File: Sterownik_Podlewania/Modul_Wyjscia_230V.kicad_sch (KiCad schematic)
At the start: 10 parts, among them J2 Screw_Terminal_01x02, K2 SANYOU_SRD_Form_C, Q2 BC547, SW8 SW_Nidec_CAS-120A1

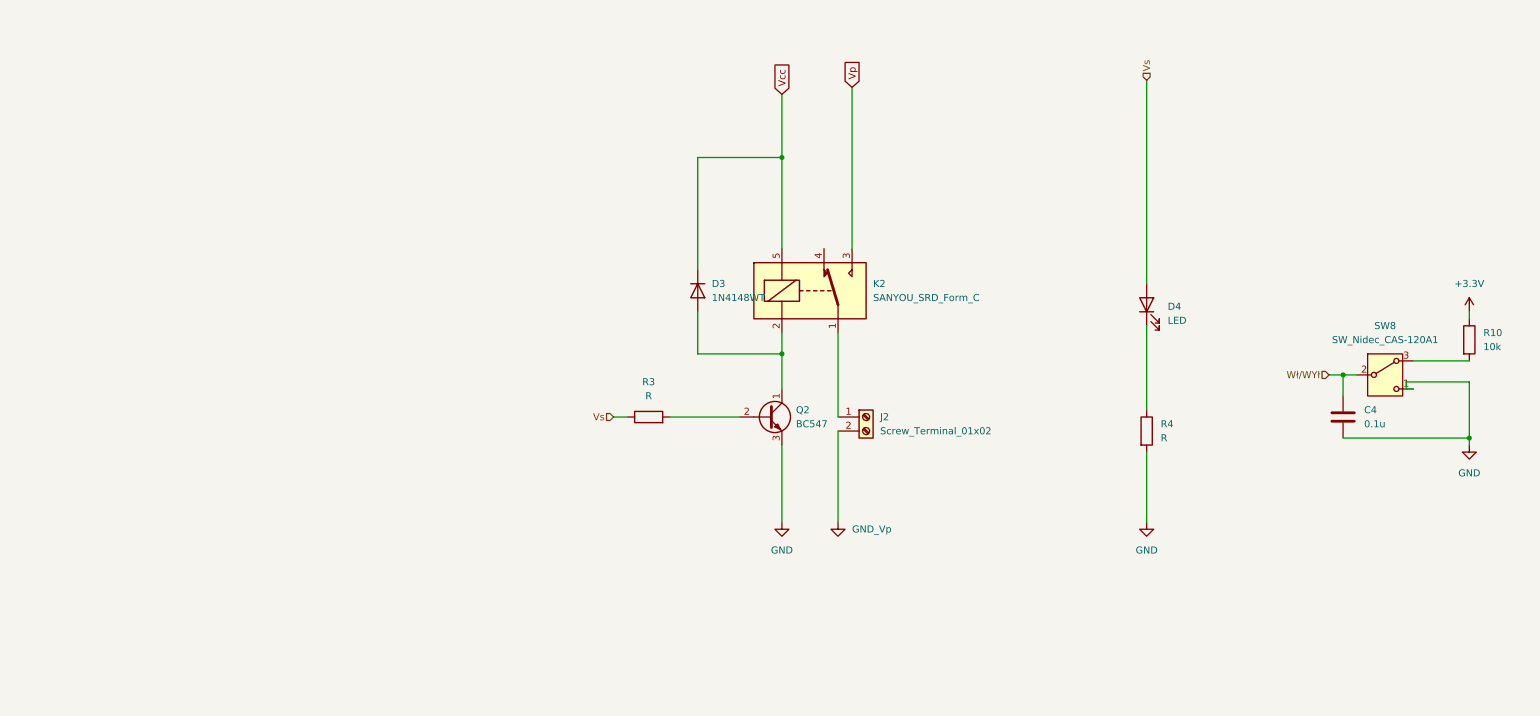
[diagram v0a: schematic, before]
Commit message: Dodanie większośi footprinów, dodanie osobno sekcji na 230V, dodanie jacka DC
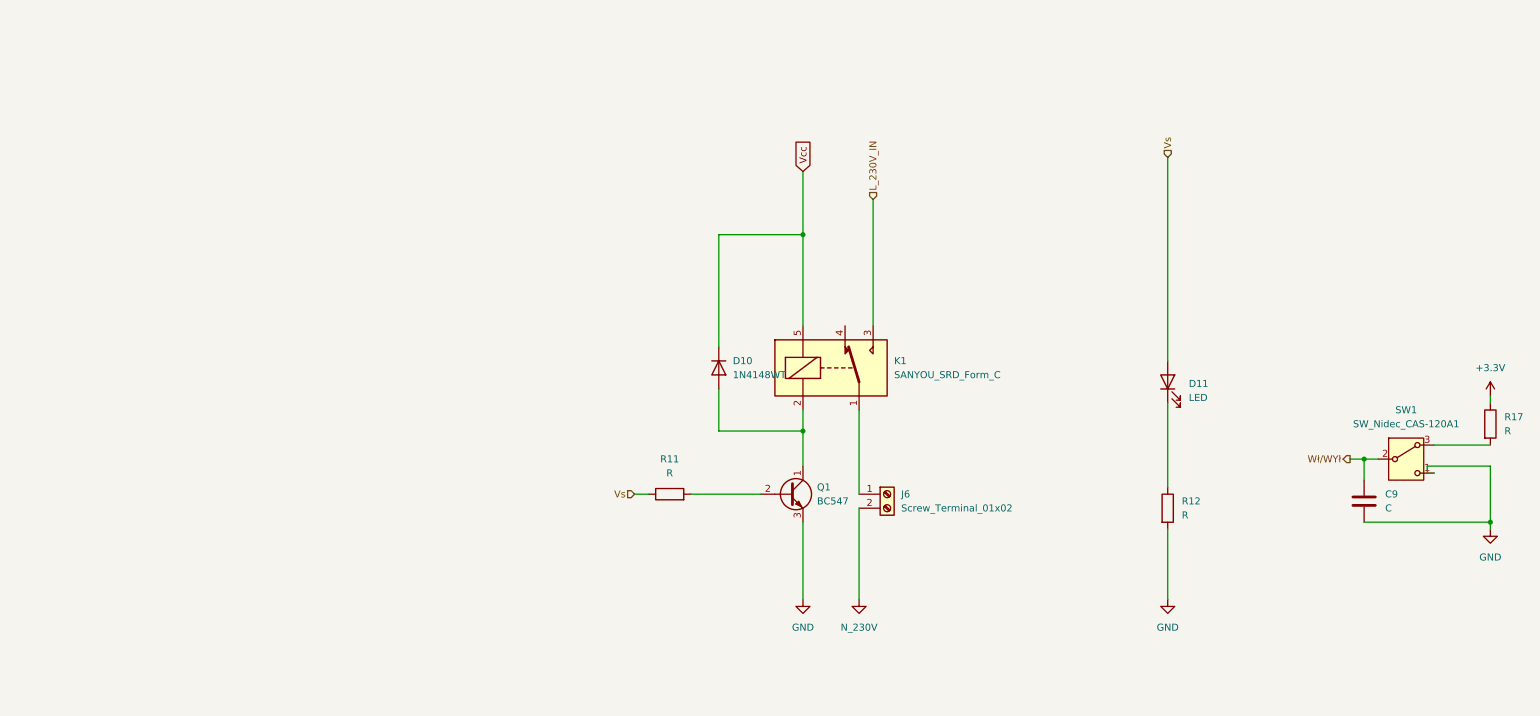
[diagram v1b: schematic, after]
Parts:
- removed C4: 0.1u, Capacitor_SMD:C_1206_3216Metric, symbol Device:C
- removed D3: 1N4148WT, Diode_SMD:D_SOD-523, symbol Diode:1N4148WT
- removed D4: LED, LED_SMD:LED_1206_3216Metric, symbol Device:LED
- removed J2: Screw_Terminal_01x02, TerminalBlock:TerminalBlock_MaiXu_MX126-5.0-02P_1x02_P5.00mm, symbol Connector:Screw_Terminal_01x02
- removed K2: SANYOU_SRD_Form_C, Relay_THT:Relay_SPDT_SANYOU_SRD_Series_Form_C, symbol Relay:SANYOU_SRD_Form_C
- removed Q2: BC547, Package_TO_SOT_THT:TO-92_Inline, symbol Transistor_BJT:BC547
- removed R10: 10k, Resistor_SMD:R_1206_3216Metric, symbol Device:R
- removed R3, R4: R, Resistor_SMD:R_1206_3216Metric, symbol Device:R
- removed SW8: SW_Nidec_CAS-120A1, Button_Switch_SMD:Nidec_Copal_CAS-120A, symbol Switch:SW_Nidec_CAS-120A1
- added C9: C, symbol Device:C
- added D10: 1N4148WT, Diode_SMD:D_SOD-523, symbol Diode:1N4148WT
- added D11: LED, LED_SMD:LED_1206_3216Metric, symbol Device:LED
- added J6: Screw_Terminal_01x02, TerminalBlock:TerminalBlock_Wuerth_691311400102_P7.62mm, symbol Connector:Screw_Terminal_01x02
- added K1: SANYOU_SRD_Form_C, Relay_THT:Relay_SPDT_SANYOU_SRD_Series_Form_C, symbol Relay:SANYOU_SRD_Form_C
- added Q1: BC547, Package_TO_SOT_THT:TO-92_Inline, symbol Transistor_BJT:BC547
- added R11, R12, R17: R, Resistor_SMD:R_1206_3216Metric, symbol Device:R
- added SW1: SW_Nidec_CAS-120A1, Button_Switch_SMD:Nidec_Copal_CAS-120A, symbol Switch:SW_Nidec_CAS-120A1
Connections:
- net +3.3V: now also R17.1
- net GND: now also C9.2, Q1.3 (E), R12.2, SW1.1 (C)
- net Vcc: now also D10.1 (K), K1.5
- net Vs: now also D11.2 (A), R11.1
- net Wł/WYł: now also C9.1, SW1.2 (B)
- new net: D10.2 (A), K1.2, Q1.1 (C)
- new net: J6.1 (Pin_1), K1.1
- new net: R17.2, SW1.3 (A)
- new net: Q1.2 (B), R11.2
- new net: D11.1 (K), R12.1
- new net L_230V_IN: K1.3
- new net N_230V: J6.2 (Pin_2)

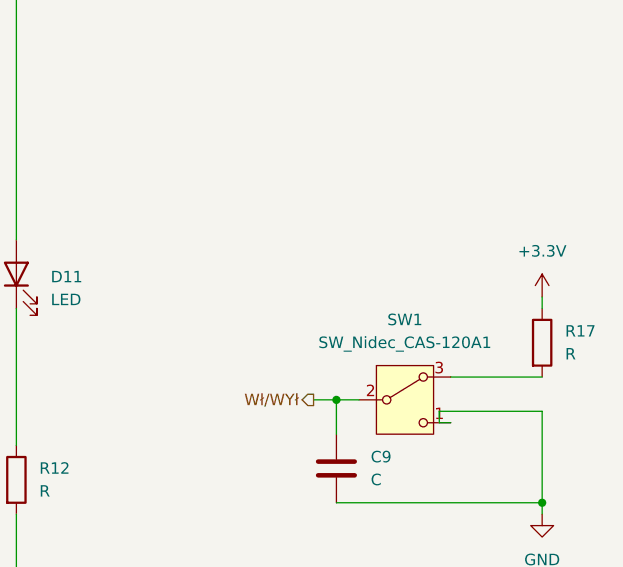
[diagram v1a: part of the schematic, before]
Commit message: Dodanie dokumentacji przełączników, sprawdzenie konwertera I2C, dodanie sekcji przełącznika, dodanie DIP swticha do przełączania zasialania zew, wydzielenie sekcji zasilania
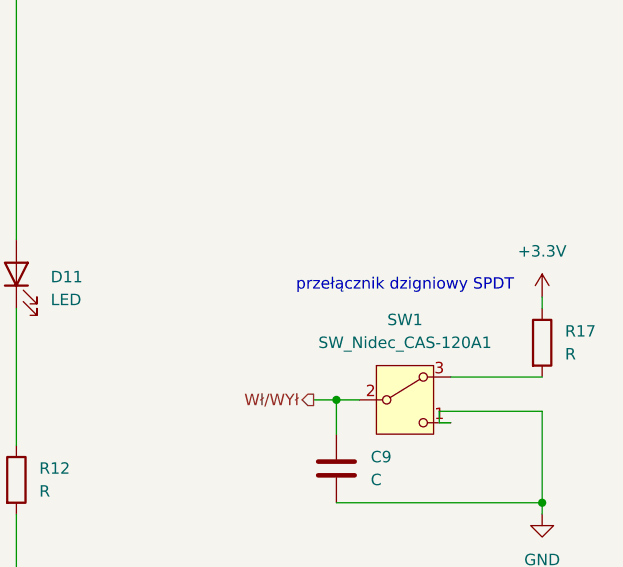
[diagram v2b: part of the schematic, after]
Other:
- note added: "przełącznik dzigniowy SPDT"
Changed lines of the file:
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@@
 	(generator_version "9.0")
 	(paper "A4")
+	(text "przełącznik dzigniowy SPDT "
+		(exclude_from_sim no)
+		(at 250.19 91.44 0)
+		(effects
+			(font
+				(size 1.27 1.27)
+			)
+			(href "https://botland.com.pl/przelaczniki-dzwigienkowe/2478-przelacznik-dzwigniowy-on-on-250v-3a-5szt-5904422356361.html")
+		)
+	)
 	(junction
 		(at 265.43 115.57)

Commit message: Poprawki estetyczne schematu
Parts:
- removed C9: C, symbol Device:C
- removed D10: 1N4148WT, Diode_SMD:D_SOD-523, symbol Diode:1N4148WT
- removed D11: LED, LED_SMD:LED_1206_3216Metric, symbol Device:LED
- removed J6: Screw_Terminal_01x02, TerminalBlock:TerminalBlock_Wuerth_691311400102_P7.62mm, symbol Connector:Screw_Terminal_01x02
- removed K1: SANYOU_SRD_Form_C, Relay_THT:Relay_SPDT_SANYOU_SRD_Series_Form_C, symbol Relay:SANYOU_SRD_Form_C
- removed Q1: BC547, Package_TO_SOT_THT:TO-92_Inline, symbol Transistor_BJT:BC547
- removed R11, R12, R17: R, Resistor_SMD:R_1206_3216Metric, symbol Device:R
- removed SW1: SW_Nidec_CAS-120A1, Button_Switch_SMD:Nidec_Copal_CAS-120A, symbol Switch:SW_Nidec_CAS-120A1
- added D15: LED, LED_SMD:LED_1206_3216Metric, symbol Device:LED
- added D9: 1N4148WT, Diode_SMD:D_SOD-523, symbol Diode:1N4148WT
- added J1: Screw_Terminal_01x02, TerminalBlock:TerminalBlock_MaiXu_MX126-5.0-02P_1x02_P5.00mm, symbol Connector:Screw_Terminal_01x02
- added K3: SANYOU_SRD_Form_C, Relay_THT:Relay_SPDT_SANYOU_SRD_Series_Form_C, symbol Relay:SANYOU_SRD_Form_C
- added Q3: BC547, Package_TO_SOT_THT:TO-92_Inline, symbol Transistor_BJT:BC547
- added R10: 680, Resistor_SMD:R_1206_3216Metric, symbol Device:R
- added R13: R, Resistor_SMD:R_1206_3216Metric, symbol Device:R
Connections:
- net GND: now also Q3.3 (E), R13.2
- net L_230V_IN: now also K3.3
- net N_230V: now also J1.2 (Pin_2)
- net Vcc: now also D9.1 (K), K3.5
- net Vs: now also D15.2 (A), R10.1
- new net: D9.2 (A), K3.2, Q3.1 (C)
- new net: Q3.2 (B), R10.2
- new net: D15.1 (K), R13.1
- new net: J1.1 (Pin_1), K3.1
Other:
- added sheet Przelacznik (Przelacznik.kicad_sch)
- note removed: "przełącznik dzigniowy SPDT"

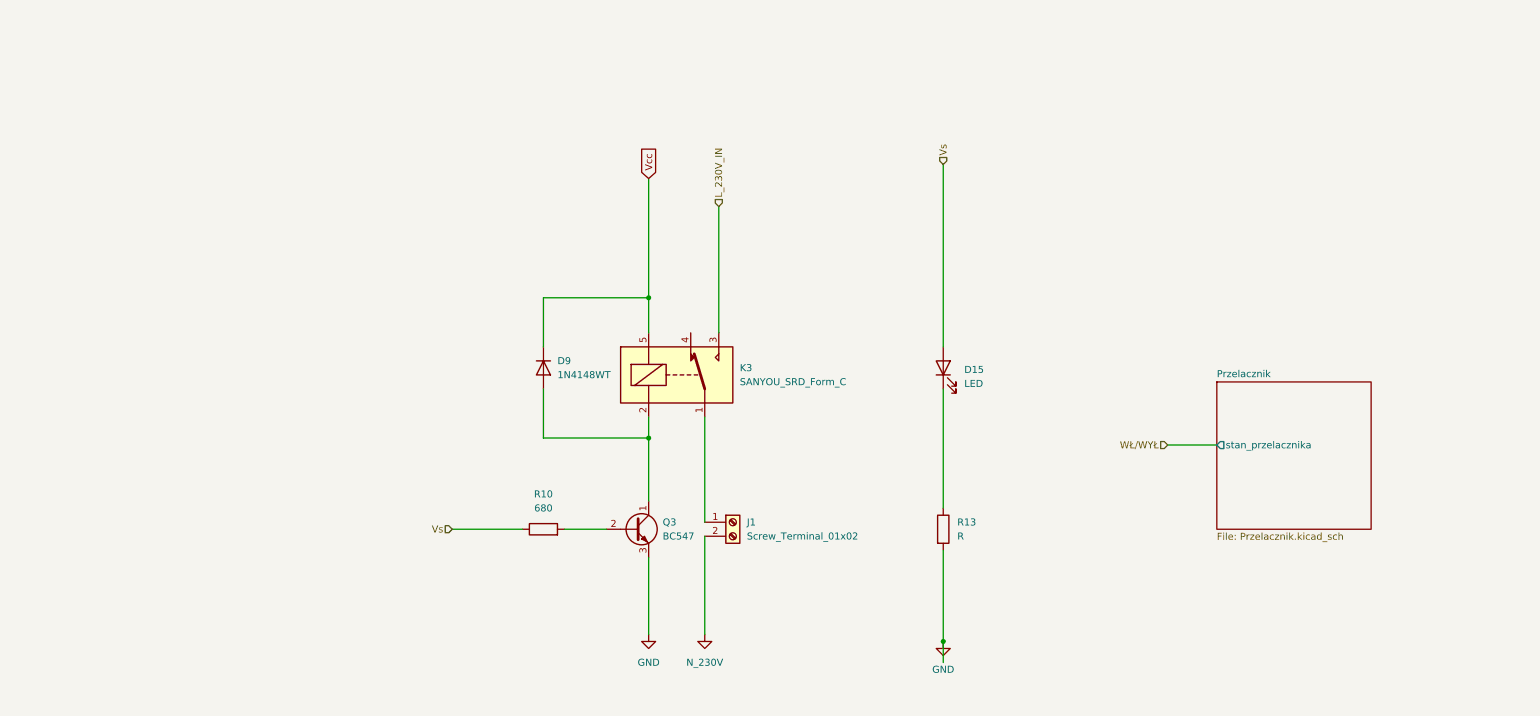
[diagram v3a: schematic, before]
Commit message: Dodanie gniazd ethernet, poprawienie większośc ERC
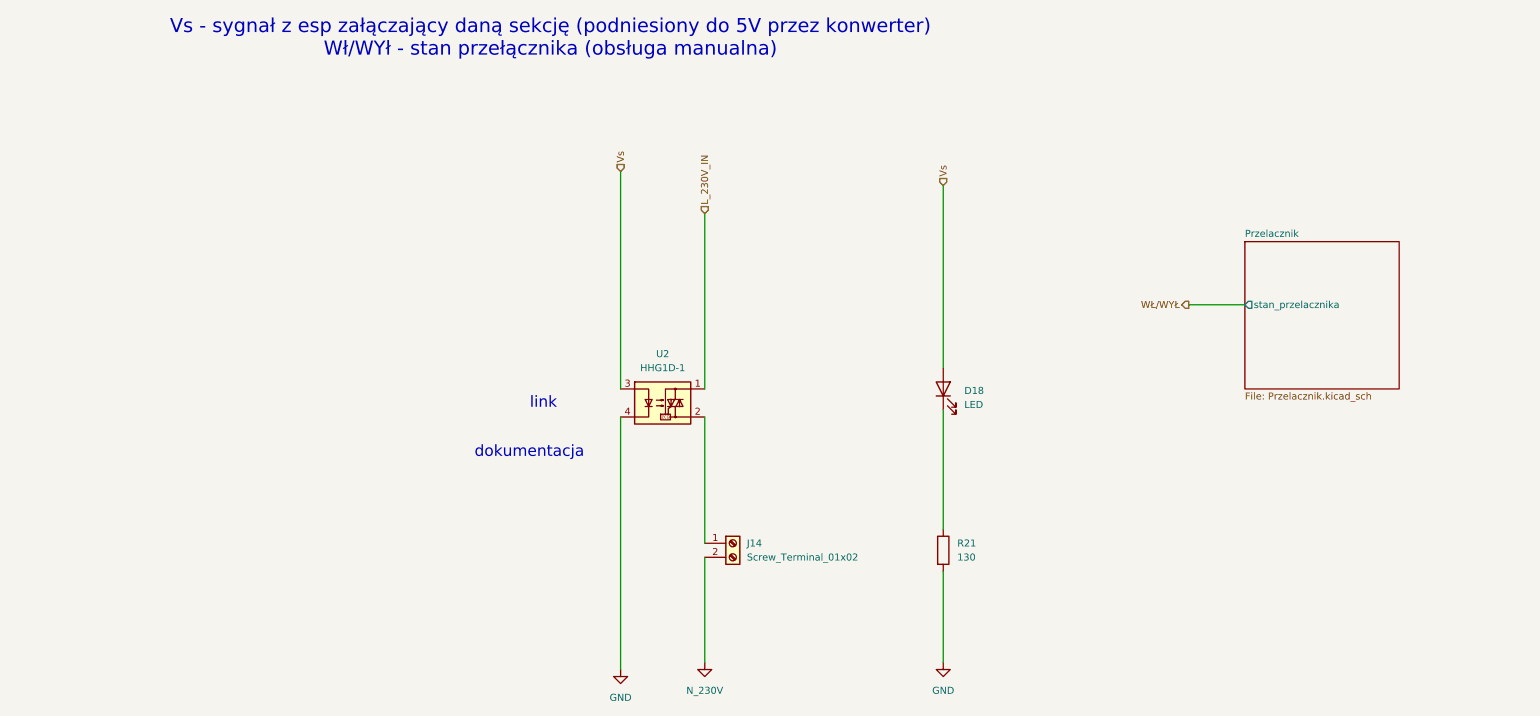
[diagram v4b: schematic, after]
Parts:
- removed D9: 1N4148WT, Diode_SMD:D_SOD-523, symbol Diode:1N4148WT
- removed K3: SANYOU_SRD_Form_C, Relay_THT:Relay_SPDT_SANYOU_SRD_Series_Form_C, symbol Relay:SANYOU_SRD_Form_C
- removed Q3: BC547, Package_TO_SOT_THT:TO-92_Inline, symbol Transistor_BJT:BC547
- removed R10: 680, Resistor_SMD:R_1206_3216Metric, symbol Device:R
- added U2: HHG1D-1, Relay_THT:Relay_NCR_HHG1D-1, symbol Relay_SolidState:HHG1D-1
- R21: renamed from R13; value R -> 130
- renumbered D15 to D18, J1 to J14
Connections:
- net GND: now also U2.4
- net L_230V_IN: now also U2.1
- net Vs: now also U2.3
- net at J14.1 (Pin_1): now also U2.2
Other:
- note added: "Vs - sygnał z esp załączający daną sekcję (podniesiony do 5V przez konwerter) Wł/WYł - stan przełącznika (obsługa manualna)"
- note added: "dokumentacja"
- note added: "link"
- title: (none) -> Sterownik podlewania V1.1
- moved on the sheet: D18, J14, R21

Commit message: Wstępny układ PCB
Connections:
- net L_230V_IN renamed 230VAC
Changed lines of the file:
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@@
-	(wire
-		(pts
-			(xy 123.19 59.69) (xy 123.19 91.44)
-		)
-		(stroke
-			(width 0)
-			(type default)
-		)
-	)
 	(wire
 		(pts
@@
 		(pts
 			(xy 166.37 124.46) (xy 166.37 140.97)
+		)
+		(stroke
+			(width 0)
+			(type default)
+		)
+	)
+	(wire
+		(pts
+			(xy 123.19 57.15) (xy 123.19 91.44)
 		)
 		(stroke
@@
 		)
 	)
-	(hierarchical_label "L_230V_IN"
-		(shape input)
-		(at 123.19 59.69 90)
-		(effects
-			(font
-				(size 1.27 1.27)
-			)
-			(justify left)
-		)
-	)
 	(hierarchical_label "WŁ{slash}WYŁ"
 		(shape output)
@@
 					(unit 1)
 				)
+			)
+		)
+	)
+	(symbol
+		(lib_id "power:AC")
+		(at 123.19 57.15 0)
+		(unit 1)
+		(exclude_from_sim no)
+		(in_bom yes)
+		(on_board yes)
+		(dnp no)
+		(fields_autoplaced yes)
+		(property "Reference" "#PWR048"
+			(at 123.19 59.69 0)
+			(effects
+				(font
+					(size 1.27 1.27)
+				)
+				(hide yes)
+			)
+		)
+		(property "Value" "230VAC"
+			(at 123.19 49.53 0)
+			(effects
+				(font
+					(size 1.27 1.27)
+				)
+			)
+		)
+		(property "Footprint" ""
+			(at 123.19 57.15 0)
+			(effects
+				(font
+					(size 1.27 1.27)
+				)
+				(hide yes)
+			)
+		)
+		(property "Datasheet" ""
+			(at 123.19 57.15 0)
+			(effects
+				(font
+					(size 1.27 1.27)
+				)
+				(hide yes)
+			)
+		)
+		(property "Description" "Power symbol creates a global label with name \"AC\""
+			(at 123.19 57.15 0)
+			(effects
+				(font
+					(size 1.27 1.27)
+				)
+				(hide yes)
+			)
+		)
+		(pin "1"
+		)
+		(instances
+			(project "Sterownik_Podlewania"
+				(path "/a66bdf1f-0e2a-4cc5-beb1-605f2a3b9885/9a88e80e-3101-4c9e-b6e9-f6fd66520dd2"
+					(reference "#PWR048")
+					(unit 1)
+				)

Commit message: Dodanie modeli 3d, nowy footprint do przełącznika, przerzucenie na drugą stronę płytki elementów, wstępne rozdzielenie elemntów pasywnych
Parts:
- U2: footprint Relay_THT:Relay_NCR_HHG1D-1 -> Relay_THT:RELAY_G3MB-202P
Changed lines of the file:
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@@
 			)
 		)
-		(property "Footprint" "Relay_THT:Relay_NCR_HHG1D-1"
+		(property "Footprint" "Relay_THT:RELAY_G3MB-202P"
 			(at 110.49 99.06 0)
 			(effects
